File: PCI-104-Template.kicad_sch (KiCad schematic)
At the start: 6 parts, among them J1 Conn_02x30_Row_Letter_First, J2 Conn_02x30_Row_Letter_First

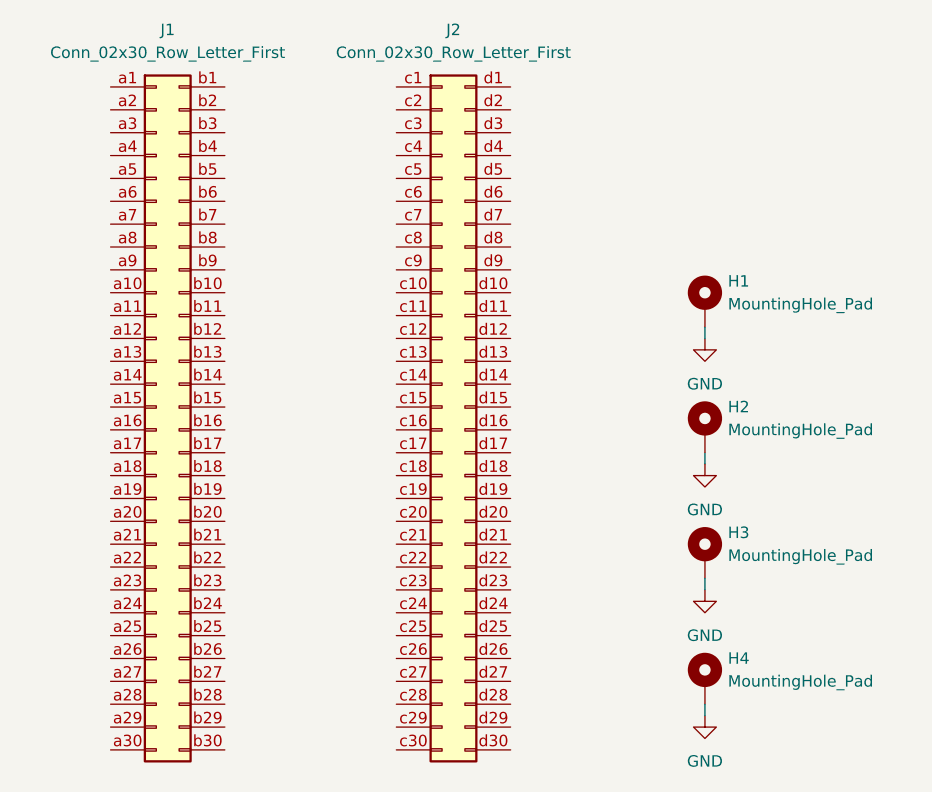
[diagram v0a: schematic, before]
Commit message: Add holes for shroud locking pegs
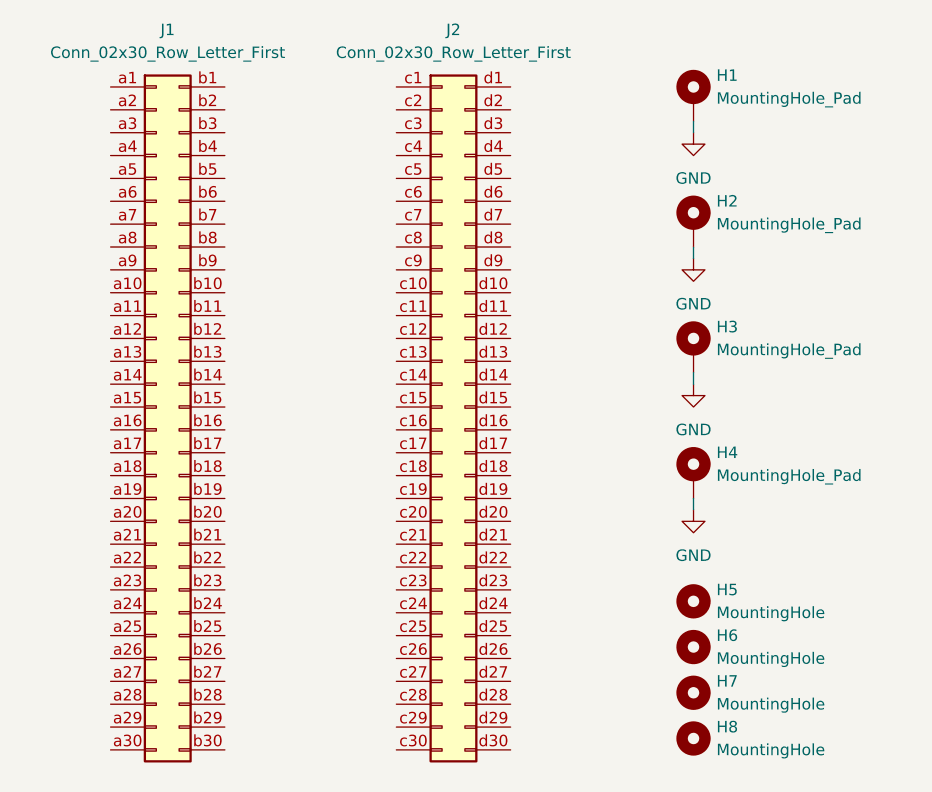
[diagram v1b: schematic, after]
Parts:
- added H5, H6, H7, H8: MountingHole, MountingHole:MountingHole_2mm, symbol Mechanical:MountingHole
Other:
- moved on the sheet: H1, H2, H3, H4
